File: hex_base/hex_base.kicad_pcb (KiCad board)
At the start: 2 copper layers, 69.3 x 80 mm, 41 parts, among them J1 ESP_proc, J10 PANEL5, J2 E75_proc, J3 USB_C, J4 PANEL0, J5 PANEL0, J6 PANEL1, J7 PANEL2, J8 PANEL3, J9 PANEL4, P1 TC2030-ESP, P2 TC2030-E75, U1 ESP32-WROOM-32, U2 E75-2G4M20S, U3 AMS1117-3.3

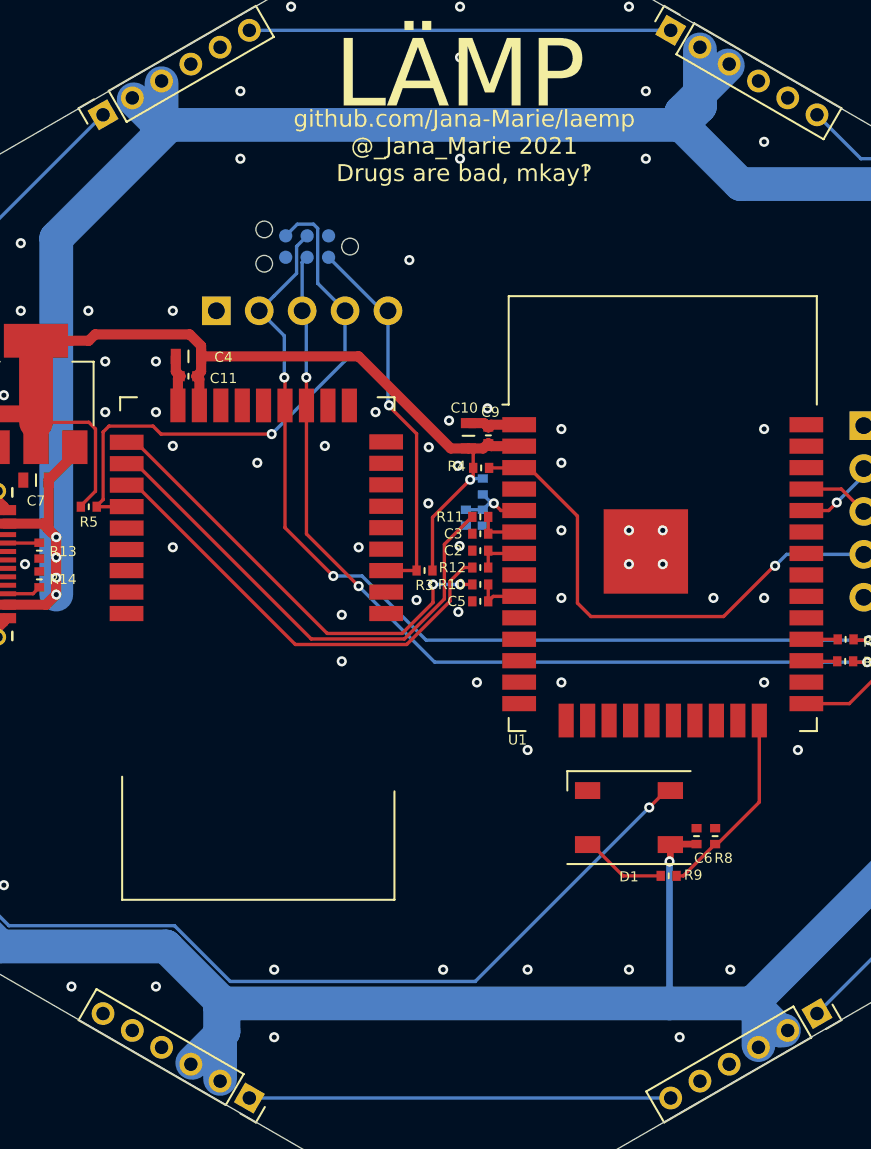
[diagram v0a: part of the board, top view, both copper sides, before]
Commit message: fitted led board onto base, todo: buttons, fix light sensor, more caps?, silkscreen
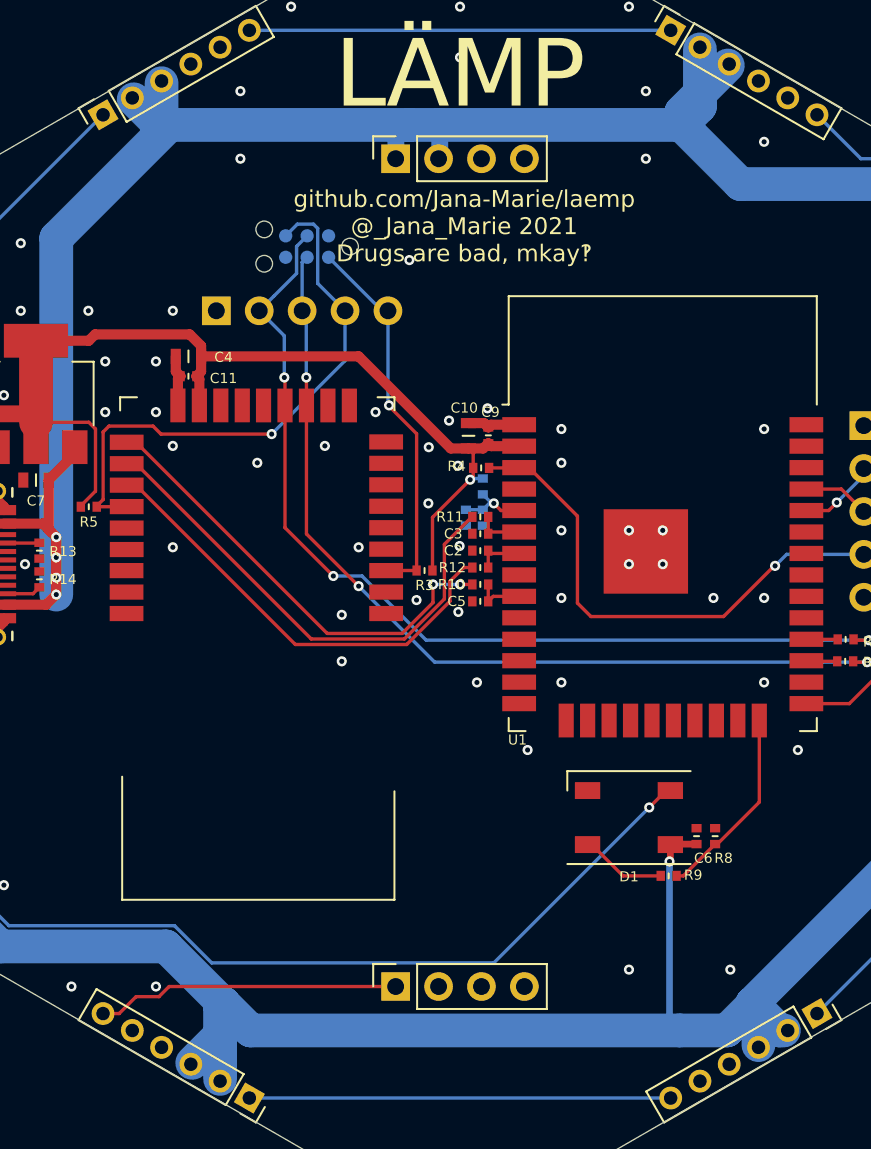
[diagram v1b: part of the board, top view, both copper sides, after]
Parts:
- added J11: LED_HEX0, otter:PinSocket_1x04_P2.54mm_Vertical_center, F.Cu at (100.0, 76.0)
- added J12: LED_HEX1, otter:PinSocket_1x04_P2.54mm_Vertical_center, F.Cu at (100.0, 125.0)
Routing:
- net DOUT: track 0.00 -> 18.0 mm
- net VBUS: track 259.2 -> 267.1 mm
- net SK6812: track 57.5 -> 56.5 mm
- net GND: vias 70 -> 64

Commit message: finished base, exported gerber
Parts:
- added C12: 100n, otter:C_0402, F.Cu at (101.2, 102.1)
- added G***: LOGO, otter:laemp_bottom_text, B.Cu at (89.8, 112.2)
- added G***: LOGO, otter:laemp_laemp, B.Cu at (112.2, 83.5)
- added R15: 100k, otter:R_0402, F.Cu at (101.2, 101.2)
- added SW1: RST, Button_Switch_SMD:SW_SPST_PTS810, B.Cu at (110.0, 100.0)
- added SW2: BIND, Button_Switch_SMD:SW_SPST_PTS810, B.Cu at (90.0, 100.0)
- C1, R2: moved to F.Cu
- R1: footprint otter:R_0402 -> otter:R_0805
- moved R10 2.75 mm to (101.2, 104.0)
- moved R2 1.96 mm to (101.2, 95.3), turned to 0 degrees
- moved C1 1.27 mm to (101.2, 96.3), turned to 180 degrees
- moved R8 1.10 mm to (115.0, 115.0)
- moved C6 1.10 mm to (114.0, 115.0)
- moved C5 0.85 mm to (101.2, 103.0)
- moved J3 0.15 mm to (72.8, 100.0)
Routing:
- net PWM_1: track 0.00 -> 21.9 mm, vias 0 -> 4
- net E75_RST: track 33.6 -> 44.9 mm
- net ESP_EN: track 36.8 -> 42.2 mm, vias 1 -> 2
- net Net-(C12-Pad1): track 0.00 -> 3.02 mm
- net +3V3: track 65.4 -> 66.4 mm
- net GND: track 9.25 -> 10.3 mm, vias 64 -> 76
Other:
- outline, holes or cut-outs redrawn
- board text added: "3V3"
- board text added: "Bind"
- board text added: "E75-2G4M20S"
- board text added: "EN"
- board text added: "ESP32"
- board text added: "GND"
- board text added: "IO0"
- board text added: "RST"
- board text added: "RX"
- board text added: "Reset"
- board text added: "TX"

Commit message: updated files
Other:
- net class Default removed

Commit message: updated file
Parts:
- added D2: D_Small, Diode_SMD:D_SOD-123F, F.Cu at (112.4, 120.2)
- added R16: DNP, otter:R_0402, F.Cu at (97.5, 123.0)
- added R17: 20, otter:R_0402, F.Cu at (97.5, 122.0)
- moved R9 2.38 mm to (110.0, 118.8), turned to -45 degrees
- turned J11 to -90 degrees
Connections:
- C6 pad 2: VBUS -> Net-(C6-Pad2)
- D1 pad 3: VBUS -> Net-(C6-Pad2)
- D1 pad 4: SK6812 -> Net-(D1-Pad4)
- J12 pad 2: Net-(J12-Pad2) -> unconnected-(J12-Pad2)
- J12 pad 3: Net-(J12-Pad3) -> unconnected-(J12-Pad3)
- J12 pad 4: Net-(J12-Pad4) -> unconnected-(J12-Pad4)
- J3 pad A6: Net-(J3-PadA6) -> unconnected-(J3-PadA6)
- J3 pad A7: Net-(J3-PadA7) -> unconnected-(J3-PadA7)
- J3 pad A8: Net-(J3-PadA8) -> unconnected-(J3-PadA8)
- J3 pad B6: Net-(J3-PadB6) -> unconnected-(J3-PadB6)
- J3 pad B7: Net-(J3-PadB7) -> unconnected-(J3-PadB7)
- J3 pad B8: Net-(J3-PadB8) -> unconnected-(J3-PadB8)
- P1 pad 1: Net-(P1-Pad1) -> unconnected-(P1-Pad1)
- P2 pad 2: Net-(P2-Pad2) -> unconnected-(P2-Pad2)
- U1 pad 10: Net-(U1-Pad10) -> unconnected-(U1-Pad10)
- U1 pad 11: Net-(U1-Pad11) -> unconnected-(U1-Pad11)
- U1 pad 12: Net-(U1-Pad12) -> unconnected-(U1-Pad12)
- U1 pad 13: Net-(U1-Pad13) -> unconnected-(U1-Pad13)
- U1 pad 14: Net-(U1-Pad14) -> unconnected-(U1-Pad14)
- U1 pad 16: Net-(U1-Pad16) -> unconnected-(U1-Pad16)
- U1 pad 17: Net-(U1-Pad17) -> unconnected-(U1-Pad17)
- U1 pad 18: Net-(U1-Pad18) -> unconnected-(U1-Pad18)
- U1 pad 19: Net-(U1-Pad19) -> unconnected-(U1-Pad19)
- U1 pad 20: Net-(U1-Pad20) -> unconnected-(U1-Pad20)
- U1 pad 21: Net-(U1-Pad21) -> unconnected-(U1-Pad21)
- U1 pad 22: Net-(U1-Pad22) -> unconnected-(U1-Pad22)
- U1 pad 23: Net-(U1-Pad23) -> unconnected-(U1-Pad23)
- U1 pad 26: Net-(U1-Pad26) -> unconnected-(U1-Pad26)
- U1 pad 29: Net-(U1-Pad29) -> unconnected-(U1-Pad29)
- U1 pad 30: Net-(U1-Pad30) -> unconnected-(U1-Pad30)
- U1 pad 31: Net-(U1-Pad31) -> unconnected-(U1-Pad31)
- U1 pad 32: Net-(U1-Pad32) -> unconnected-(U1-Pad32)
- U1 pad 36: Net-(U1-Pad36) -> unconnected-(U1-Pad36)
- U1 pad 37: Net-(U1-Pad37) -> unconnected-(U1-Pad37)
- U1 pad 4: Net-(U1-Pad4) -> unconnected-(U1-Pad4)
- U2 pad 1: Net-(U2-Pad1) -> unconnected-(U2-Pad1)
- U2 pad 10: Net-(U2-Pad10) -> unconnected-(U2-Pad10)
- U2 pad 11: Net-(U2-Pad11) -> unconnected-(U2-Pad11)
- U2 pad 14: Net-(U2-Pad14) -> unconnected-(U2-Pad14)
- U2 pad 15: Net-(U2-Pad15) -> unconnected-(U2-Pad15)
- U2 pad 2: Net-(U2-Pad2) -> unconnected-(U2-Pad2)
- U2 pad 23: Net-(U2-Pad23) -> unconnected-(U2-Pad23)
- U2 pad 24: Net-(U2-Pad24) -> unconnected-(U2-Pad24)
- U2 pad 25: Net-(U2-Pad25) -> unconnected-(U2-Pad25)
- U2 pad 4: Net-(U2-Pad4) -> unconnected-(U2-Pad4)
- U2 pad 5: Net-(U2-Pad5) -> unconnected-(U2-Pad5)
- U2 pad 6: Net-(U2-Pad6) -> unconnected-(U2-Pad6)
- U2 pad 7: Net-(U2-Pad7) -> unconnected-(U2-Pad7)
- U2 pad 8: Net-(U2-Pad8) -> unconnected-(U2-Pad8)
- U2 pad 9: Net-(U2-Pad9) -> unconnected-(U2-Pad9)
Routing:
- net Net-(D1-Pad4): track 0.00 -> 19.2 mm, vias 0 -> 2
- net SK6812: track 56.5 -> 37.6 mm
- net VBUS: track 267.6 -> 262.4 mm
- net Net-(R8-Pad2): track 11.2 -> 15.6 mm
- net Net-(C6-Pad2): track 0.00 -> 4.02 mm
- net DOUT: track 18.0 -> 20.3 mm
- net Net-(D1-Pad2): track 5.10 -> 2.87 mm
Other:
- board text added: "JLCJLCJLCJLC"
- board text added: "github.com/Jana-Marie/laemp @_Jana_Marie 2022 v1.2 Drugs are bad, mkay‽"
- board text removed: "github.com/Jana-Marie/laemp @_Jana_Marie 2021 Drugs are bad, mkay‽"
